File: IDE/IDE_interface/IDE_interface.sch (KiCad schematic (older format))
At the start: 16 parts, among them P1 EXPANSION PORT, P2 IDE0, U1 74LS32, U2 74LS139, U3 74HC74, U4 74LS08, U5 DS1511Y+, U6 74LS574, U7 74LS574, U8 74HC245

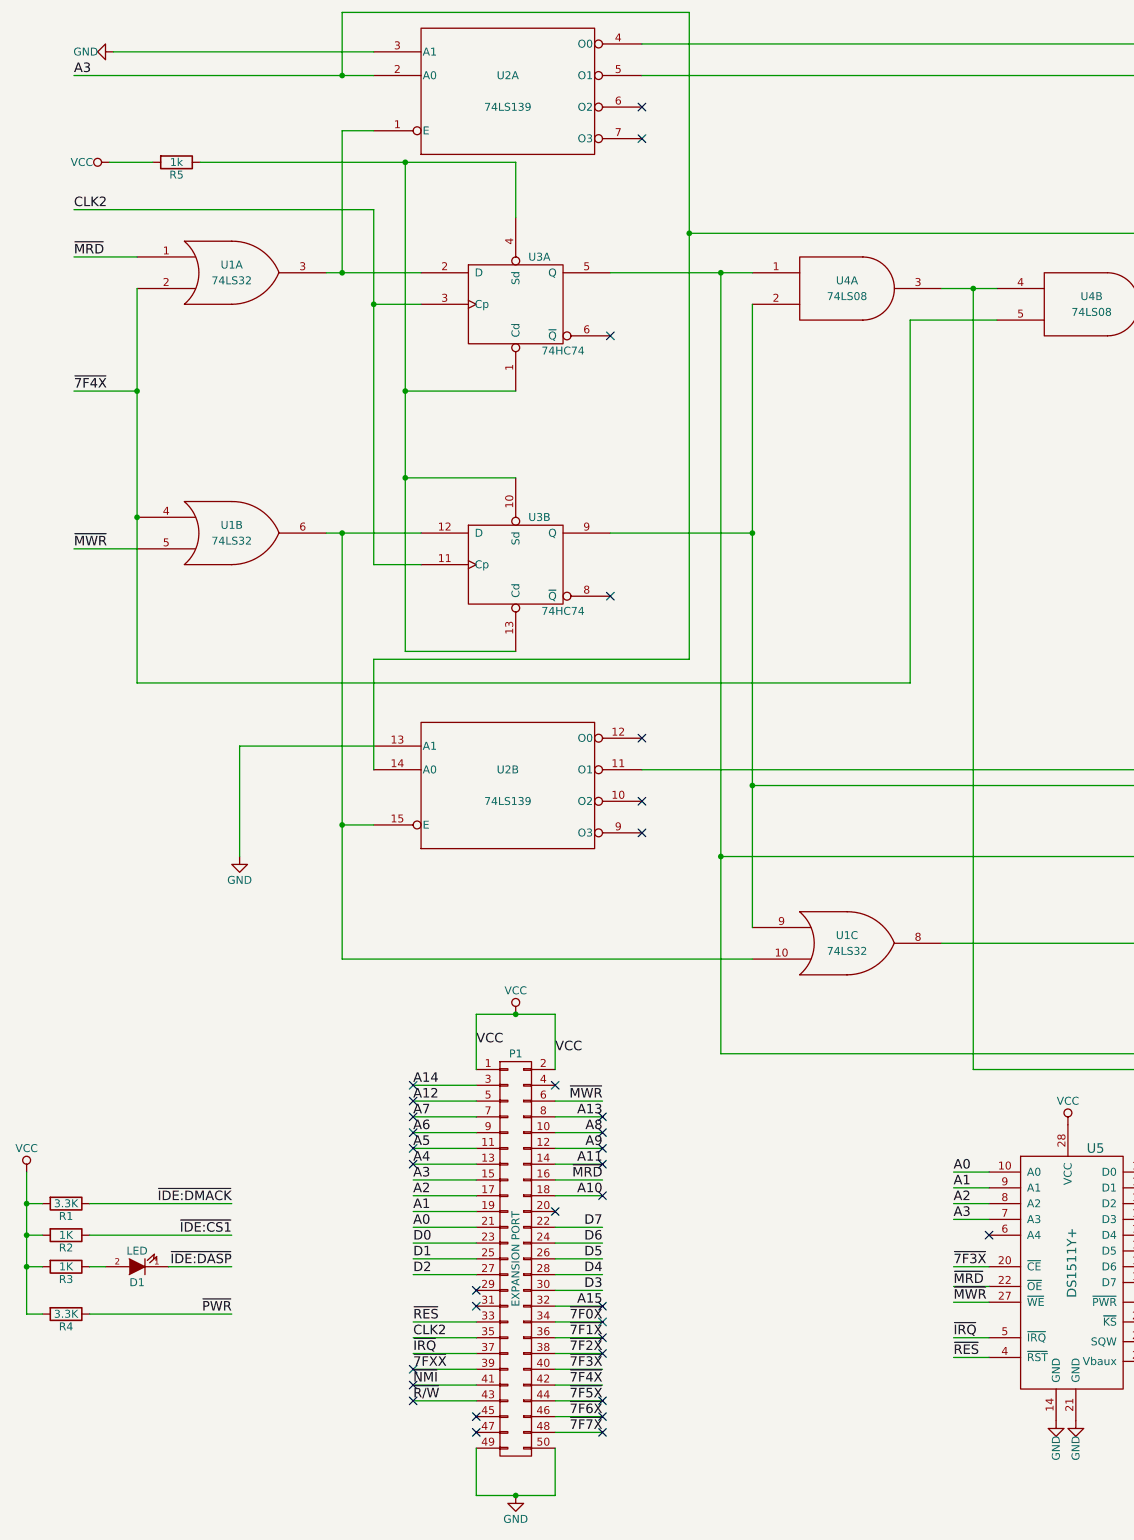
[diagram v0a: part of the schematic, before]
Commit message: Changed names of IO select lines.
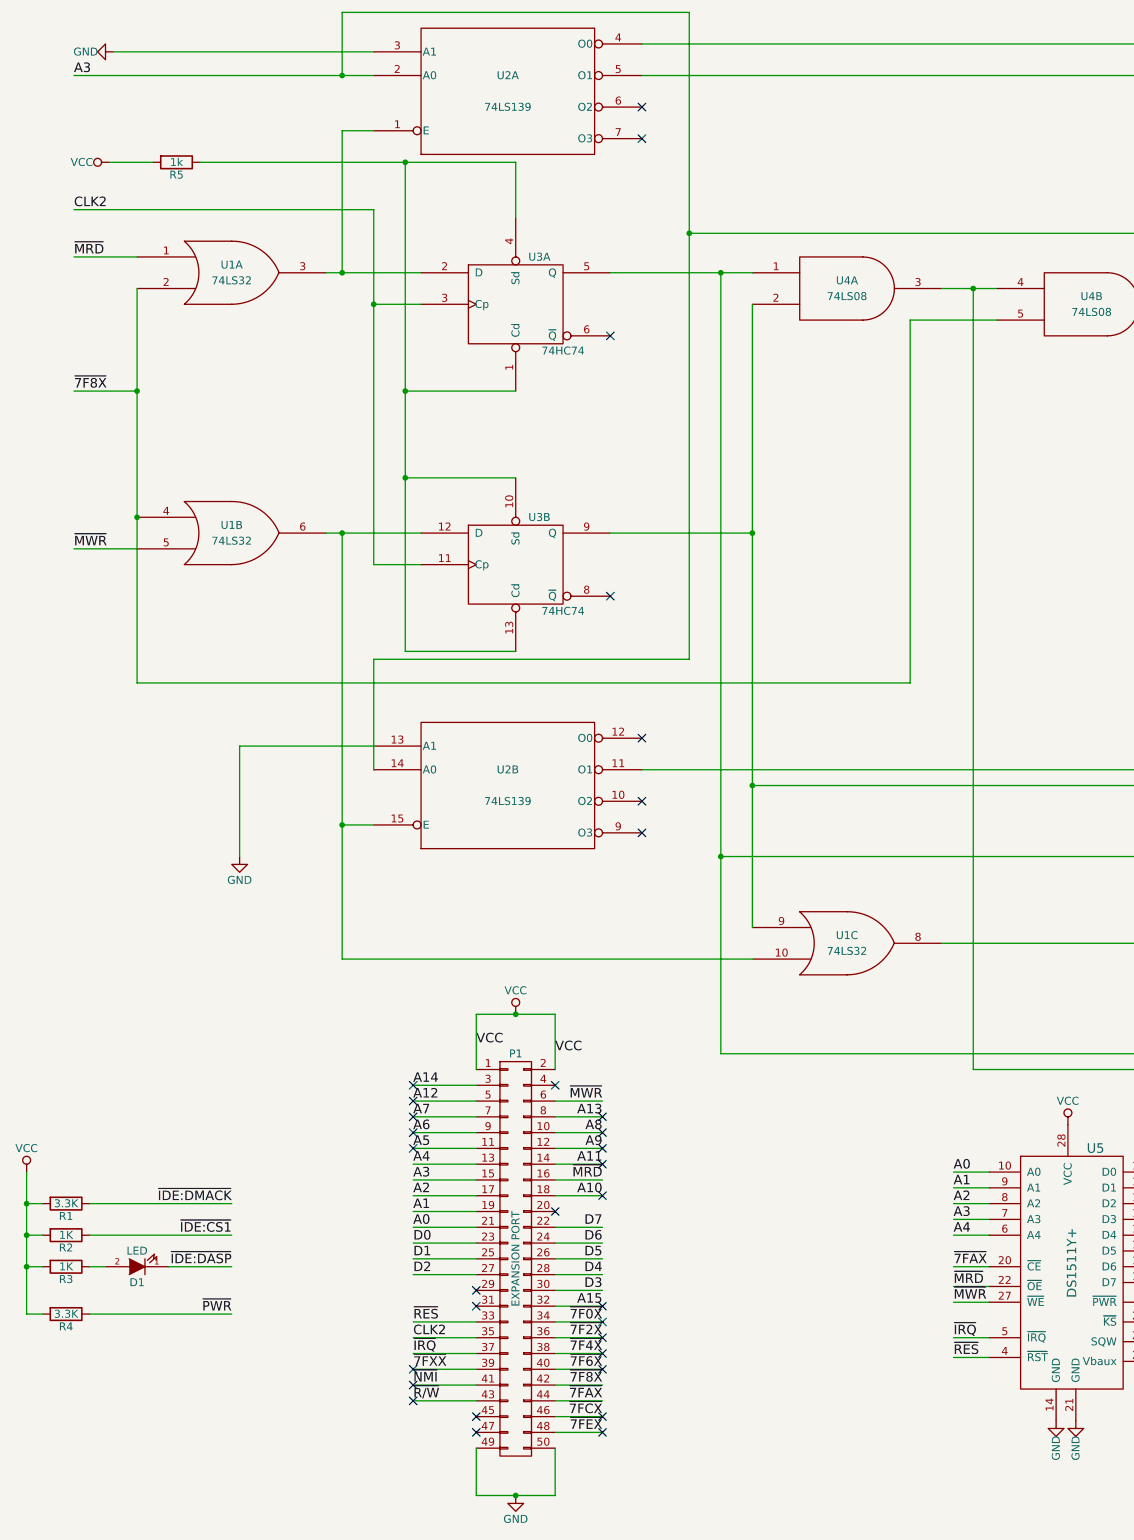
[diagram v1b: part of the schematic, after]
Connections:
- net ~7F1X is gone; now on net ~7F2X: P1.36 (P36)
- net ~7F5X is gone; now on net ~7FAX: P1.44 (P44)
- net A4: now also U5.6 (A4)
- net ~7F2X: no longer P1.38 (P38)
- net ~7F4X: now also P1.38 (P38); no longer P1.42 (P42), U1.2, U1.4, U4.5
- net ~7F6X: now also P1.40 (P40); no longer P1.46 (P46)
- net ~7F3X renamed ~7FAX
- net ~7FAX: no longer P1.40 (P40)
- net ~7F7X renamed ~7FEX
- new net ~7F8X: P1.42 (P42), U1.2, U1.4, U4.5
- new net ~7FCX: P1.46 (P46)
- no-connect marks 42 -> 40
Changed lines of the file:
@@
 LIBS:valves
 LIBS:IDE_interface
+LIBS:65xx
 LIBS:IDE_interface-cache
 EELAYER 25 0
@@
 ~7F0X
 Text Label 4450 9100 2    60   ~ 0
-~7F1X
+~7F2X
 Text Label 4450 9200 2    60   ~ 0
-~7F2X
+~7F4X
 Text Label 4450 9300 2    60   ~ 0
-~7F3X
+~7F6X
 Text Label 4450 9400 2    60   ~ 0
-~7F4X
+~7F8X
 Text Label 4450 9500 2    60   ~ 0
-~7F5X
+~7FAX
 Text Label 4450 9600 2    60   ~ 0
-~7F6X
+~7FCX
 Text Label 4450 9700 2    60   ~ 0
-~7F7X
+~7FEX
 Text Label 15750 2700 2    60   ~ 0
 ~IDE:CS1
@@
 NoConn ~ 3250 7800
 NoConn ~ 3250 7900
-NoConn ~ 3250 8000
 NoConn ~ 4450 7700
 NoConn ~ 4450 7800
@@
 NoConn ~ 4450 8200
 NoConn ~ 4450 8900
-NoConn ~ 4450 9000
-NoConn ~ 4450 9100
-NoConn ~ 4450 9200
-NoConn ~ 4450 9500
-NoConn ~ 4450 9600
-NoConn ~ 4450 9700
 NoConn ~ 3250 9300
 NoConn ~ 3250 9400
@@
 CLK2
 Text Label 1100 3100 0    60   ~ 0
-~7F4X
+~7F8X
 Text Label 1100 4100 0    60   ~ 0
 ~MWR
@@
 Text Label 8225 8750 2    60   ~ 0
 D7
-NoConn ~ 6900 8450
 Text Label 6675 8650 0    60   ~ 0
-~7F3X
+~7FAX
 Text Label 6675 8775 0    60   ~ 0
 ~MRD
@@
 	3000 5500 3000 4800
 Wire Wire Line
-	5000 4800 3000 4800
-Wire Wire Line
-	5000 700  5000 4800
+	3000 4800 5000 4800
+Wire Wire Line
+	5000 4800 5000 700
 Wire Wire Line
 	5000 700  2800 700
@@
 	1    0    0    -1
 $EndComp
+Wire Wire Line
+	6900 8450 6675 8450
+Text Label 6675 8450 0    60   ~ 0
+A4
+NoConn ~ 4450 9000
+NoConn ~ 4450 9100
+NoConn ~ 4450 9200
+NoConn ~ 4450 9300
+NoConn ~ 4450 9600
+NoConn ~ 4450 9700
 $EndSCHEMATC
